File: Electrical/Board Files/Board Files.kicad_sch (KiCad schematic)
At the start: 6 parts

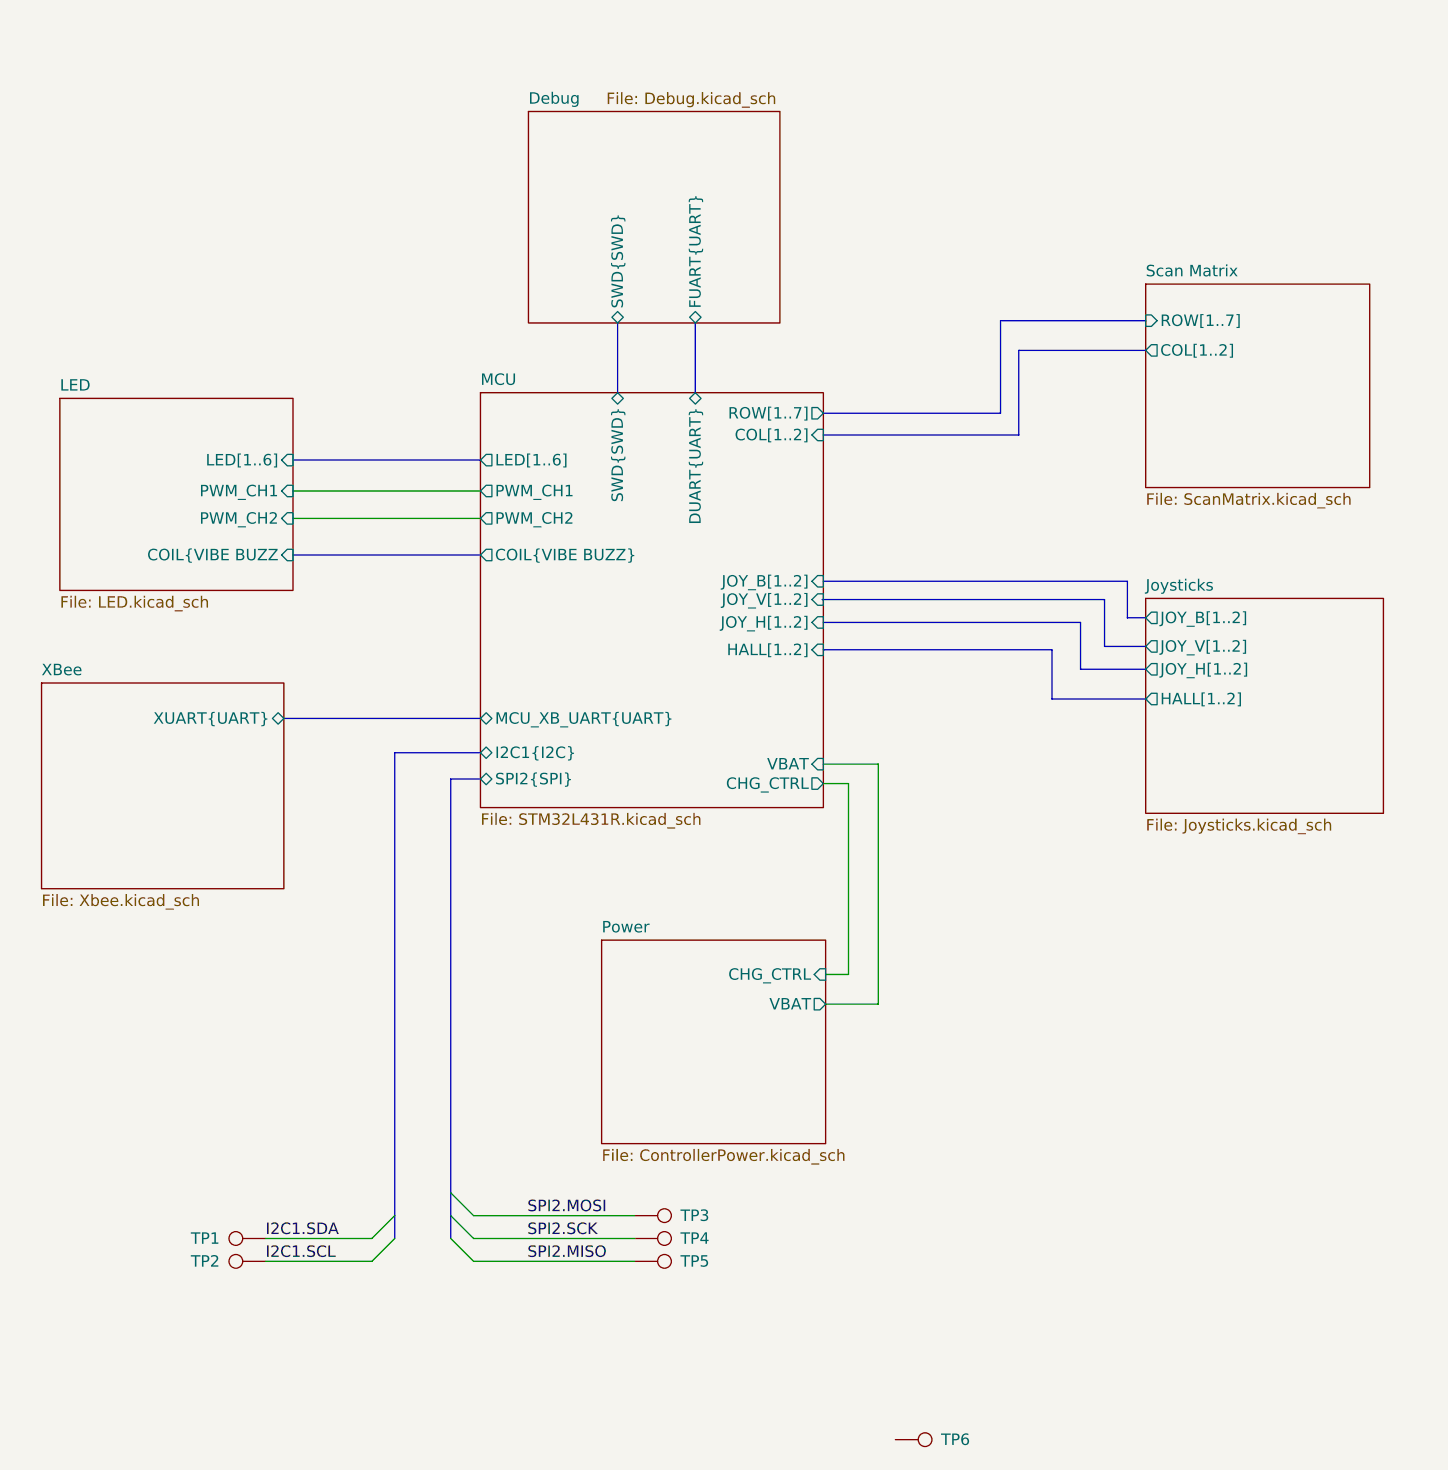
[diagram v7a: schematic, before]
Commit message: Added hall effect sensors
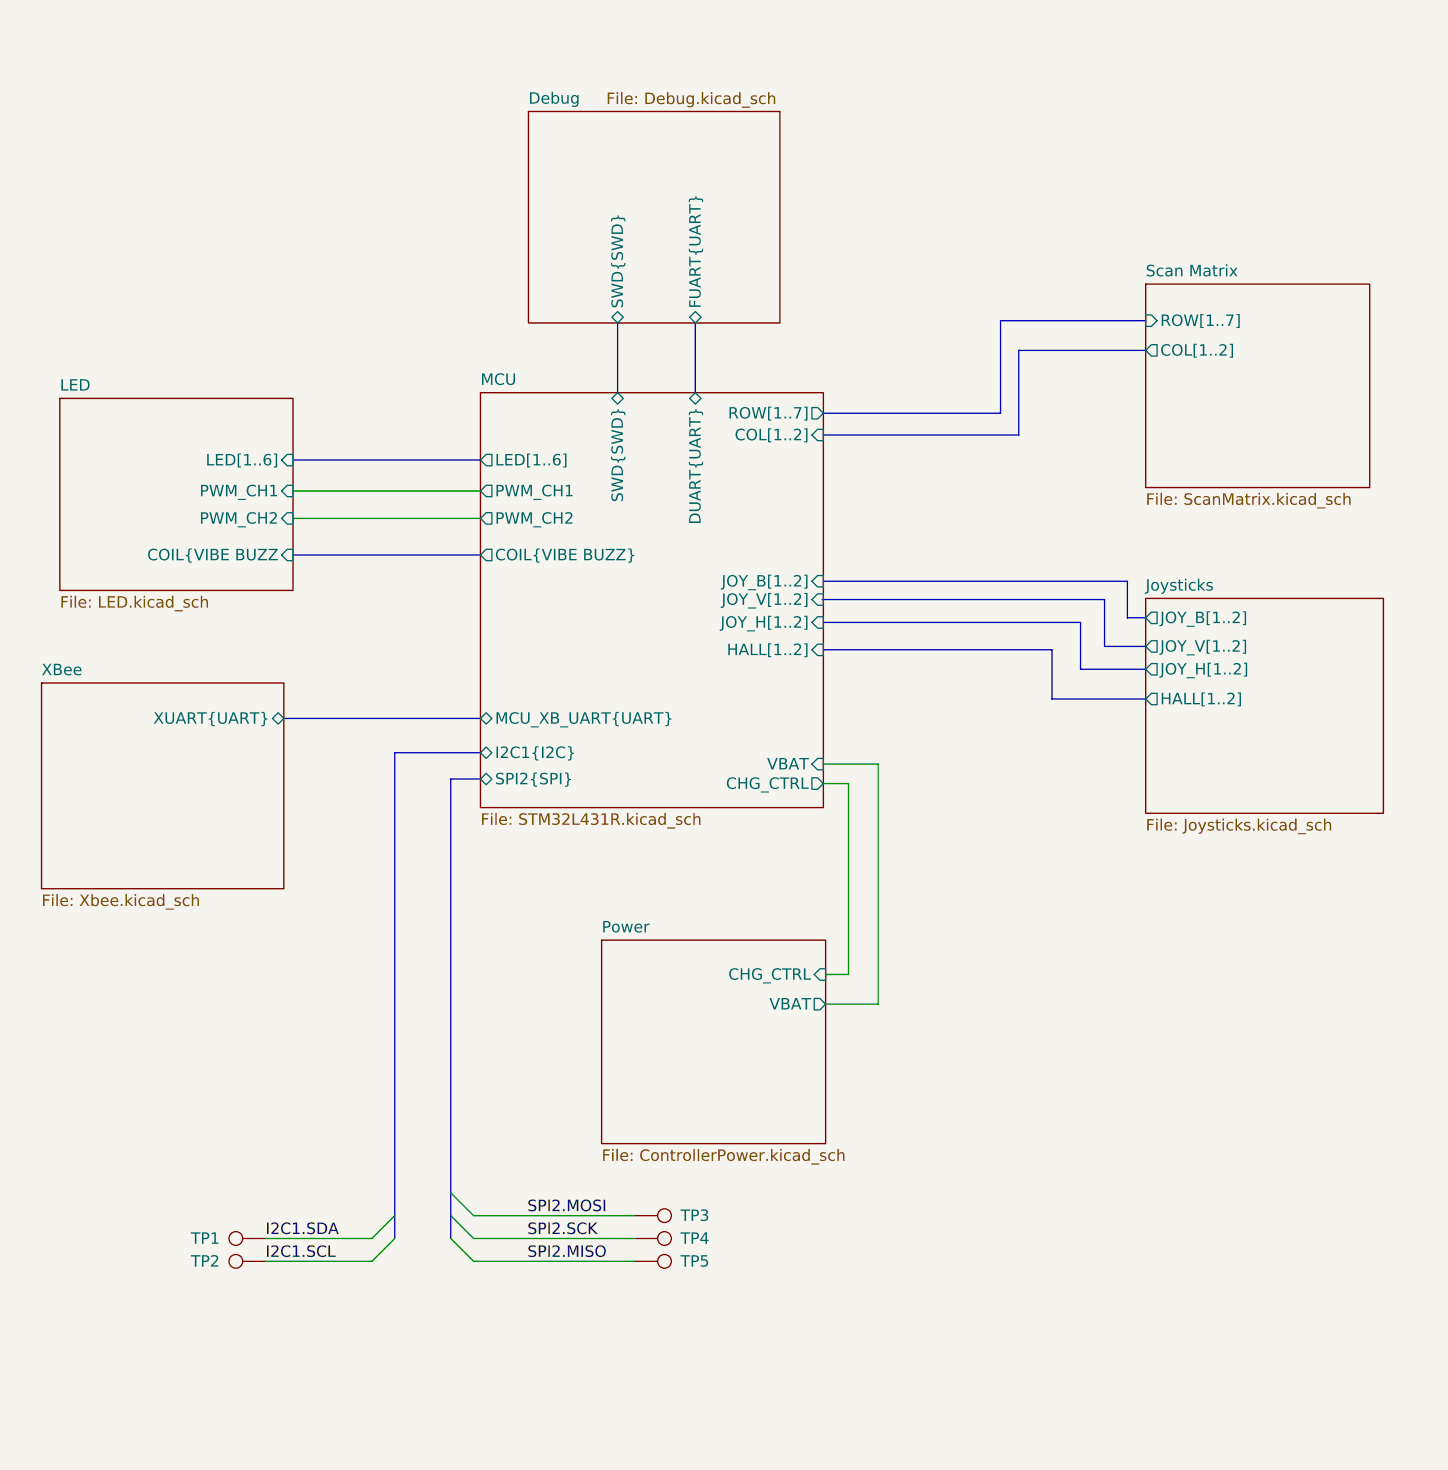
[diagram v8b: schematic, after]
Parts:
- removed TP6: ~, symbol Connector:TestPoint
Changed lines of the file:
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@@
     (stroke (width 0) (type default) (color 0 0 0 0))
   )
-  (bus (pts (xy 93.345 80.01) (xy 114.046 80.01))
+  (bus (pts (xy 93.218 80.01) (xy 114.046 80.01))
     (stroke (width 0) (type default) (color 0 0 0 0))
   )
@@
     )
     (property "Datasheet" "~" (id 3) (at 131.191 169.037 0)
-      (effects (font (size 1.27 1.27)) hide)
-    )
-    (pin "1")
-  )
-  (symbol (lib_id "Connector:TestPoint") (at 160.147 188.849 270) (unit 1)
-    (in_bom yes) (on_board yes)
-    (property "Reference" "TP6" (id 0) (at 165.227 188.8489 90)
-      (effects (font (size 1.27 1.27)) (justify left))
-    )
-    (property "Value" "~" (id 1) (at 165.227 190.1189 90)
-      (effects (font (size 1.27 1.27)) (justify left))
-    )
-    (property "Footprint" "" (id 2) (at 160.147 193.929 0)
-      (effects (font (size 1.27 1.27)) hide)
-    )
-    (property "Datasheet" "~" (id 3) (at 160.147 193.929 0)
       (effects (font (size 1.27 1.27)) hide)
     )
@@
   )
   (symbol_instances
+    (path "/899d6960-0494-4e8f-9091-802503c02d1b/05ad0275-f781-4be4-98eb-989604fb05a9"
+      (reference "#FLG0101") (unit 1) (value "PWR_FLAG") (footprint "")
+    )
     (path "/899d6960-0494-4e8f-9091-802503c02d1b/b6f4ec66-a1ed-4e6d-8017-469a52f8ebbb"
       (reference "#PWR01") (unit 1) (value "VCC") (footprint "")
@@
       (reference "#PWR046") (unit 1) (value "~") (footprint "")
     )
+    (path "/761fe907-e5d9-42db-98c6-e1ff4e3d741c/8506198c-e487-433c-aab7-286ef4f95195"
+      (reference "#PWR047") (unit 1) (value "+3V3") (footprint "")
+    )
+    (path "/761fe907-e5d9-42db-98c6-e1ff4e3d741c/c96f38eb-5b0e-4012-8f7b-433b57c4fdd5"
+      (reference "#PWR048") (unit 1) (value "GND") (footprint "")
+    )
+    (path "/761fe907-e5d9-42db-98c6-e1ff4e3d741c/db8c97fe-31ce-4561-a5db-99ce9d98704e"
+      (reference "#PWR049") (unit 1) (value "+3V3") (footprint "")
+    )
+    (path "/761fe907-e5d9-42db-98c6-e1ff4e3d741c/ee833407-5781-4488-a398-1ae7451b0ad0"
+      (reference "#PWR050") (unit 1) (value "GND") (footprint "")
+    )
     (path "/be02c95d-2968-40ec-875d-106e3ff13333/6ef1c94a-5d04-44b4-8be3-ff213f767449"
       (reference "BZ1") (unit 1) (value "Buzzer") (footprint "")
@@
       (reference "C36") (unit 1) (value "1u") (footprint "")
     )
+    (path "/761fe907-e5d9-42db-98c6-e1ff4e3d741c/baabcf94-9598-4025-962f-8f575dcd309a"
+      (reference "C37") (unit 1) (value "1u") (footprint "")
+    )
+    (path "/761fe907-e5d9-42db-98c6-e1ff4e3d741c/b379fbbc-01e4-4e89-95cf-d8fe8ad3854a"
+      (reference "C38") (unit 1) (value "0.01u") (footprint "")
+    )
+    (path "/761fe907-e5d9-42db-98c6-e1ff4e3d741c/7ea3f923-8211-456a-ad0c-07739ea063db"
+      (reference "C39") (unit 1) (value "1u") (footprint "")
+    )
+    (path "/761fe907-e5d9-42db-98c6-e1ff4e3d741c/7c9e6d79-377e-48f0-a29a-559ba80fcd14"
+      (reference "C40") (unit 1) (value "0.01u") (footprint "")
+    )
     (path "/e322e877-fa4b-40a1-b9eb-04bd2db5ed6c/71ae1396-694c-4f1a-8dbc-510787c9338c"
       (reference "D1") (unit 1) (value "~") (footprint "")
@@
       (reference "TP5") (unit 1) (value "~") (footprint "")
     )
-    (path "/c0279923-cf62-4e35-b55d-ece4bb190210"
-      (reference "TP6") (unit 1) (value "~") (footprint "")
-    )
     (path "/899d6960-0494-4e8f-9091-802503c02d1b/7d042535-a9b1-4541-bdce-2605e3a8d022"
       (reference "TP7") (unit 1) (value "~") (footprint "")
@@
       (reference "U8") (unit 1) (value "FT231XS") (footprint "Package_SO:SSOP-20_3.9x8.7mm_P0.635mm")
     )
-  )
+    (path "/761fe907-e5d9-42db-98c6-e1ff4e3d741c/7eb0bda8-bd9b-4b1a-a008-9cb25ee8bb0c"
+      (reference "U9") (unit 1) (value "DRV5055A2xLPGxQ1") (footprint "Package_TO_SOT_THT:TO-92_Inline")
+    )
+    (path "/761fe907-e5d9-42db-98c6-e1ff4e3d741c/bc671941-dc5d-4a4d-ab2d-fc9a81dde6c9"
+      (reference "U10") (unit 1) (value "DRV5055A2xLPGxQ1") (footprint "Package_TO_SOT_THT:TO-92_Inline")
+    )
+  )
